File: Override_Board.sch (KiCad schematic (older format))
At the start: 11 parts

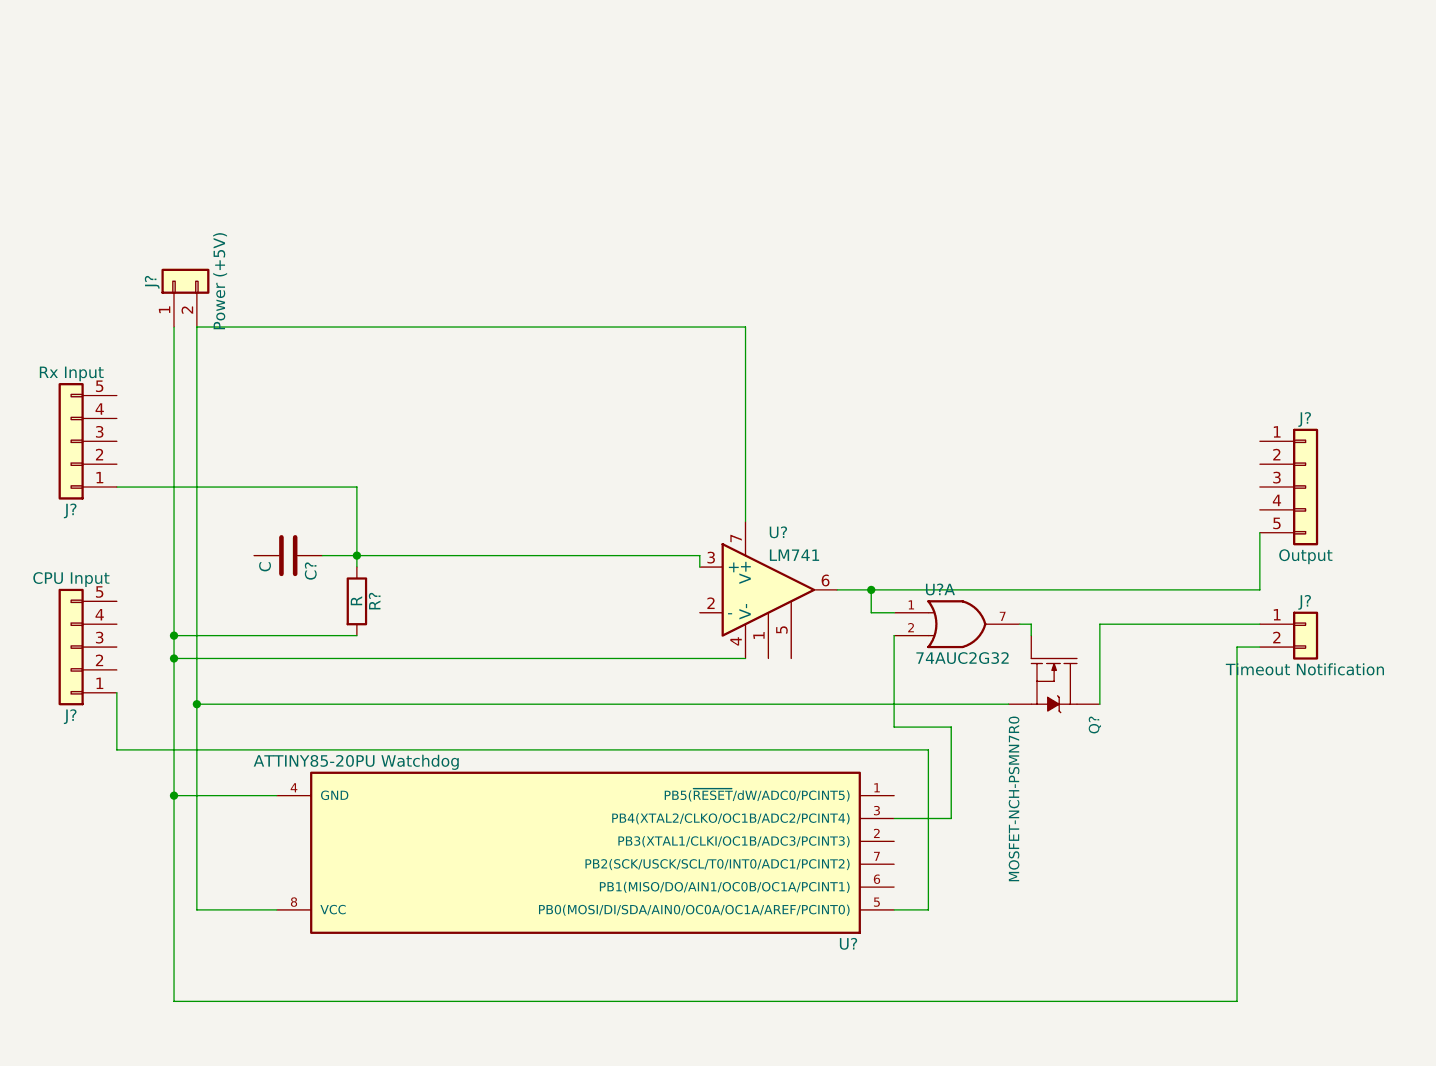
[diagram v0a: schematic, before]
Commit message: Added mux into circuit design
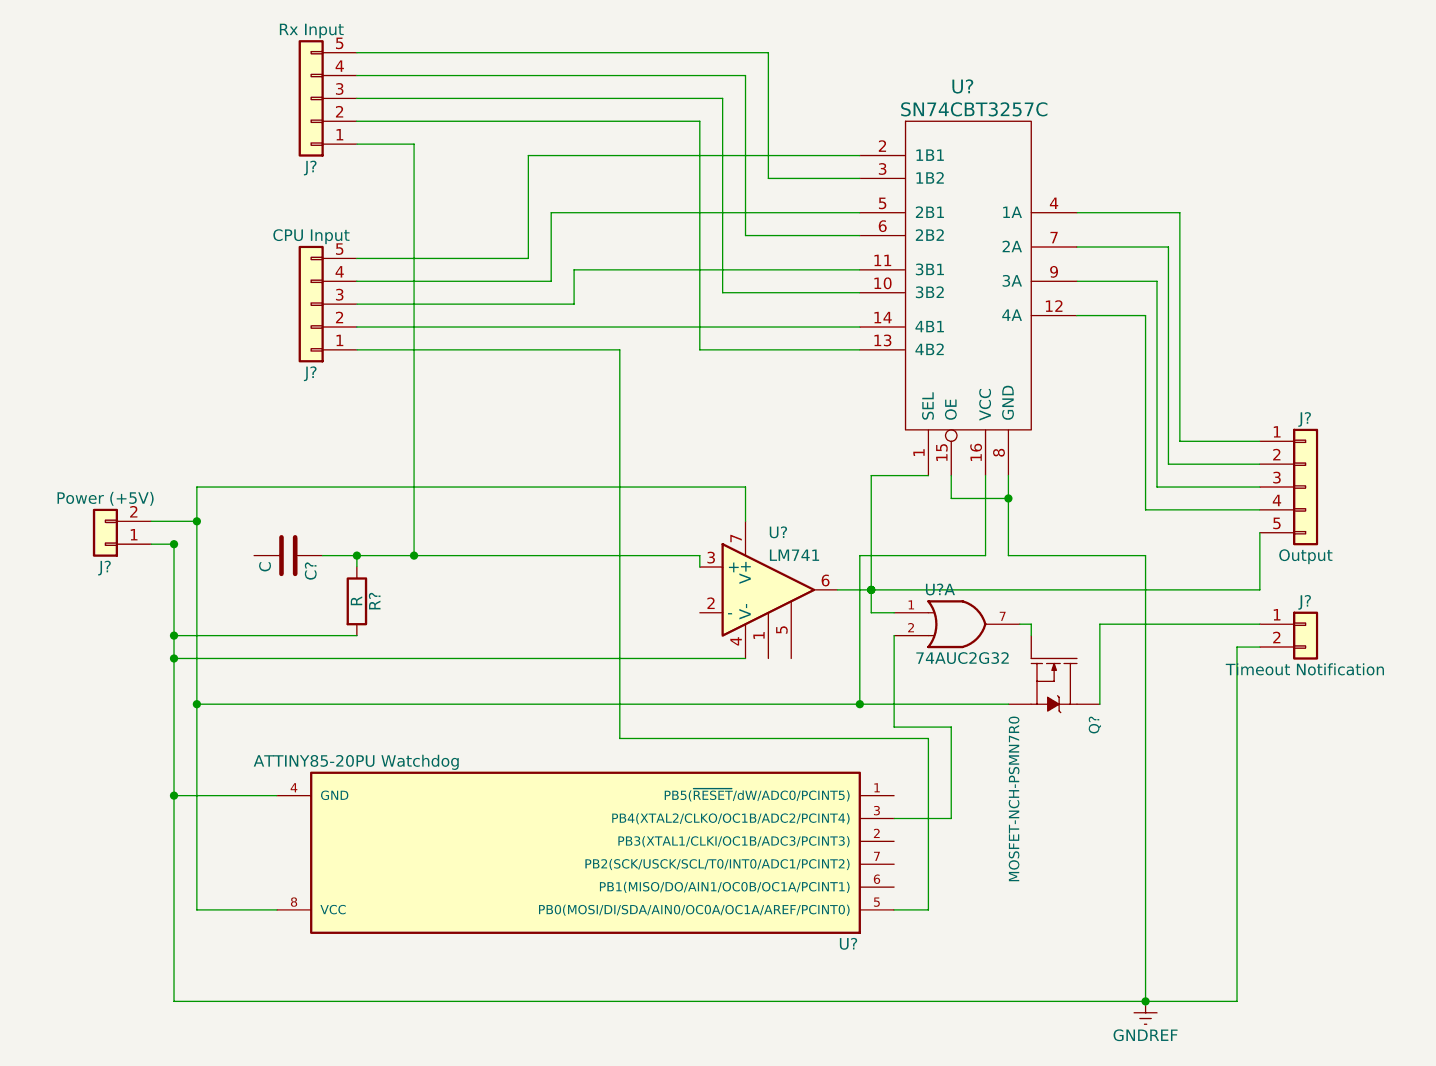
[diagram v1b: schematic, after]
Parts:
- added U?: SN74CBT3257C, symbol SN74CBT3257C
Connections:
- net at J?.2 (Pin_2): now also U?.14 (4B1)
- net at J?.3 (Pin_3): now also U?.11 (3B1)
- net at J?.4 (Pin_4): now also U?.5 (2B1)
- net at J?.5 (Pin_5): now also U?.2 (1B1)
- net at J?.1 (Pin_1): now also U?.4 (1A)
- net at J?.2 (Pin_2): now also U?.7 (2A)
- net at J?.3 (Pin_3): now also U?.9 (3A)
- net at J?.4 (Pin_4): now also U?.12 (4A)
- net at J?.5 (Pin_5), U?.1, U?.6: now also U?.1 (SEL)
- net GNDREF: now reaches J?.1 (Pin_1), J?.2 (Pin_2), R?.2, U?.4 (GND), U?.4 (V-)
- net GNDREF: now also U?.15 (OE), U?.8 (GND)
- net at J?.2 (Pin_2), Q?.3 (S), U?.7 (V+)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: now also U?.16 (VCC)
- net at J?.2 (Pin_2): now also U?.13 (4B2)
- net at J?.3 (Pin_3): now also U?.10 (3B2)
- net at J?.4 (Pin_4): now also U?.6 (2B2)
- net at J?.5 (Pin_5): now also U?.3 (1B2)
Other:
- moved on the sheet: J?
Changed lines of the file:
@@
 LIBS:SparkFun-Sensors
 LIBS:SparkFun-Switches
+LIBS:ugl
+LIBS:sn74cbt3257c
+LIBS:Override_Board-cache
 EELAYER 25 0
 EELAYER END
@@
 L Conn_01x05 J?
 U 1 1 5AA19F29
-P 4500 3300
-F 0 "J?" H 4500 3600 50  0000 C CNN
-F 1 "CPU Input" H 4500 3000 50  0000 C CNN
-F 2 "" H 4500 3300 50  0001 C CNN
-F 3 "" H 4500 3300 50  0001 C CNN
-	1    4500 3300
+P 5550 1800
+F 0 "J?" H 5550 2100 50  0000 C CNN
+F 1 "CPU Input" H 5550 1500 50  0000 C CNN
+F 2 "" H 5550 1800 50  0001 C CNN
+F 3 "" H 5550 1800 50  0001 C CNN
+	1    5550 1800
 	-1   0    0    1
 $EndComp
@@
 L Conn_01x02 J?
 U 1 1 5AA1A099
-P 4950 1700
-F 0 "J?" H 4950 1800 50  0000 C CNN
-F 1 "Power (+5V)" H 4950 1500 50  0000 C CNN
-F 2 "" H 4950 1700 50  0001 C CNN
-F 3 "" H 4950 1700 50  0001 C CNN
-	1    4950 1700
-	0    -1   -1   0
+P 4650 2850
+F 0 "J?" H 4650 2950 50  0000 C CNN
+F 1 "Power (+5V)" H 4650 2650 50  0000 C CNN
+F 2 "" H 4650 2850 50  0001 C CNN
+F 3 "" H 4650 2850 50  0001 C CNN
+	1    4650 2850
+	-1   0    0    1
 $EndComp
 $Comp
 L Conn_01x05 J?
 U 1 1 5AA1A1A7
-P 4500 2400
-F 0 "J?" H 4500 2700 50  0000 C CNN
-F 1 "Rx Input" H 4500 2100 50  0000 C CNN
-F 2 "" H 4500 2400 50  0001 C CNN
-F 3 "" H 4500 2400 50  0001 C CNN
-	1    4500 2400
+P 5550 900
+F 0 "J?" H 5550 1200 50  0000 C CNN
+F 1 "Rx Input" H 5550 600 50  0000 C CNN
+F 2 "" H 5550 900 50  0001 C CNN
+F 3 "" H 5550 900 50  0001 C CNN
+	1    5550 900
 	-1   0    0    1
 $EndComp
@@
 $EndComp
 Wire Wire Line
-	5050 1900 5050 4450
+	5050 2600 5050 2750
+Wire Wire Line
+	5050 2750 5050 3550
+Wire Wire Line
+	5050 3550 5050 4450
 Wire Wire Line
 	5050 4450 5400 4450
@@
 	4950 3950 5400 3950
 Wire Wire Line
-	4950 1900 4950 4850
+	4950 2850 4950 3250
+Wire Wire Line
+	4950 3250 4950 3350
+Wire Wire Line
+	4950 3350 4950 3950
+Wire Wire Line
+	4950 3950 4950 4850
 Wire Wire Line
 	9700 3300 9600 3300
@@
 	9600 3300 9600 4850
 Wire Wire Line
-	9600 4850 4950 4850
+	9600 4850 9200 4850
+Wire Wire Line
+	9200 4850 4950 4850
 Connection ~ 4950 3950
 $Comp
@@
 	9000 3200 9000 3550
 Wire Wire Line
-	8600 3550 5050 3550
+	5050 3550 7950 3550
+Wire Wire Line
+	7950 3550 8600 3550
 Connection ~ 5050 3550
 Wire Wire Line
-	4700 3500 4700 3750
-Wire Wire Line
-	4700 3750 8250 3750
-Wire Wire Line
-	8250 3750 8250 4450
+	8250 3700 8250 4450
 Wire Wire Line
 	8250 4450 8100 4450
 Wire Wire Line
-	9700 2800 9700 3050
-Wire Wire Line
-	9700 3050 7850 3050
+	9700 3050 9700 2800
+Wire Wire Line
+	7850 3050 8000 3050
+Wire Wire Line
+	8000 3050 8000 3050
+Wire Wire Line
+	8000 3050 9700 3050
 $Comp
 L LM741 U?
@@
 $EndComp
 Wire Wire Line
-	7450 2750 7450 1900
-Wire Wire Line
-	7450 1900 5050 1900
+	7450 2750 7450 2600
+Wire Wire Line
+	7450 2600 5050 2600
 Wire Wire Line
 	7450 3350 4950 3350
@@
 $EndComp
 Wire Wire Line
-	4700 2600 5750 2600
-Wire Wire Line
-	5750 2600 5750 2950
-Wire Wire Line
-	5600 2900 7250 2900
+	5600 2900 5750 2900
+Wire Wire Line
+	5750 2900 6000 2900
+Wire Wire Line
+	6000 2900 7250 2900
 Connection ~ 5750 2900
 Wire Wire Line
@@
 	8000 3150 8000 3050
 Connection ~ 8000 3050
+$Comp
+L SN74CBT3257C U?
+U 1 1 5AA1CA44
+P 8400 2350
+F 0 "U?" H 8400 3850 60  0000 C CNN
+F 1 "SN74CBT3257C" H 8450 3750 60  0000 C CNN
+F 2 "" H 8400 3850 60  0001 C CNN
+F 3 "" H 8400 3850 60  0001 C CNN
+	1    8400 2350
+	1    0    0    -1
+$EndComp
+Wire Wire Line
+	8900 1400 9350 1400
+Wire Wire Line
+	9350 1400 9350 2400
+Wire Wire Line
+	9350 2400 9700 2400
+Wire Wire Line
+	9700 2500 9300 2500
+Wire Wire Line
+	9300 2500 9300 1550
+Wire Wire Line
+	9300 1550 8900 1550
+Wire Wire Line
+	8900 1700 9250 1700
+Wire Wire Line
+	9250 1700 9250 2600
+Wire Wire Line
+	9250 2600 9700 2600
+Wire Wire Line
+	9700 2700 9200 2700
+Wire Wire Line
+	9200 2700 9200 1850
+Wire Wire Line
+	9200 1850 8900 1850
+Wire Wire Line
+	8600 2550 8600 2650
+Wire Wire Line
+	8600 2650 8600 2900
+Wire Wire Line
+	8600 2900 9200 2900
+Wire Wire Line
+	9200 2900 9200 4850
+Connection ~ 9200 4850
+Wire Wire Line
+	8500 2550 8500 2900
+Wire Wire Line
+	8500 2900 7950 2900
+Wire Wire Line
+	7950 2900 7950 3550
+Connection ~ 7950 3550
+Wire Wire Line
+	8350 2550 8350 2650
+Wire Wire Line
+	8350 2650 8600 2650
+Connection ~ 8600 2650
+Wire Wire Line
+	8250 2550 8000 2550
+Wire Wire Line
+	8000 2550 8000 3050
+Connection ~ 8000 3050
+Wire Wire Line
+	5750 1100 6000 1100
+Wire Wire Line
+	6000 1100 6000 2900
+Connection ~ 6000 2900
+Wire Wire Line
+	5750 2000 6900 2000
+Wire Wire Line
+	6900 2000 6900 3700
+Wire Wire Line
+	6900 3700 8250 3700
+Wire Wire Line
+	5750 1900 7950 1900
+Wire Wire Line
+	5750 1800 6700 1800
+Wire Wire Line
+	6700 1800 6700 1650
+Wire Wire Line
+	6700 1650 7950 1650
+Wire Wire Line
+	7950 1400 6600 1400
+Wire Wire Line
+	6600 1400 6600 1700
+Wire Wire Line
+	6600 1700 5750 1700
+Wire Wire Line
+	5750 1600 6500 1600
+Wire Wire Line
+	6500 1600 6500 1150
+Wire Wire Line
+	6500 1150 7950 1150
+Wire Wire Line
+	7950 2000 7250 2000
+Wire Wire Line
+	7250 2000 7250 1000
+Wire Wire Line
+	7250 1000 5750 1000
+Wire Wire Line
+	5750 900  7350 900
+Wire Wire Line
+	7350 900  7350 1750
+Wire Wire Line
+	7350 1750 7950 1750
+Wire Wire Line
+	7950 1500 7450 1500
+Wire Wire Line
+	7450 1500 7450 800
+Wire Wire Line
+	7450 800  5750 800
+Wire Wire Line
+	7550 1250 7950 1250
+Wire Wire Line
+	7550 1250 7550 700
+Wire Wire Line
+	7550 700  5750 700
+Wire Wire Line
+	4850 2750 5050 2750
+Connection ~ 5050 2750
+Wire Wire Line
+	4850 2850 4950 2850
+Connection ~ 4950 2850
+Wire Wire Line
+	5750 2950 5750 2900
+$Comp
+L GNDREF #PWR?
+U 1 1 5AA1D8F2
+P 9200 4850
+F 0 "#PWR?" H 9200 4600 50  0001 C CNN
+F 1 "GNDREF" H 9200 4700 50  0000 C CNN
+F 2 "" H 9200 4850 50  0001 C CNN
+F 3 "" H 9200 4850 50  0001 C CNN
+	1    9200 4850
+	1    0    0    -1
+$EndComp
 $EndSCHEMATC
